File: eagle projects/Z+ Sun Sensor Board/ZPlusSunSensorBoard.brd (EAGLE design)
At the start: 78 x 78 mm, 50 parts, among them U1 TSV991AILT, U2 ADS7841E_2K5, U4 LM20BIM7X_NOPB, U5 TSV991AILT, U8 TSV991AILT

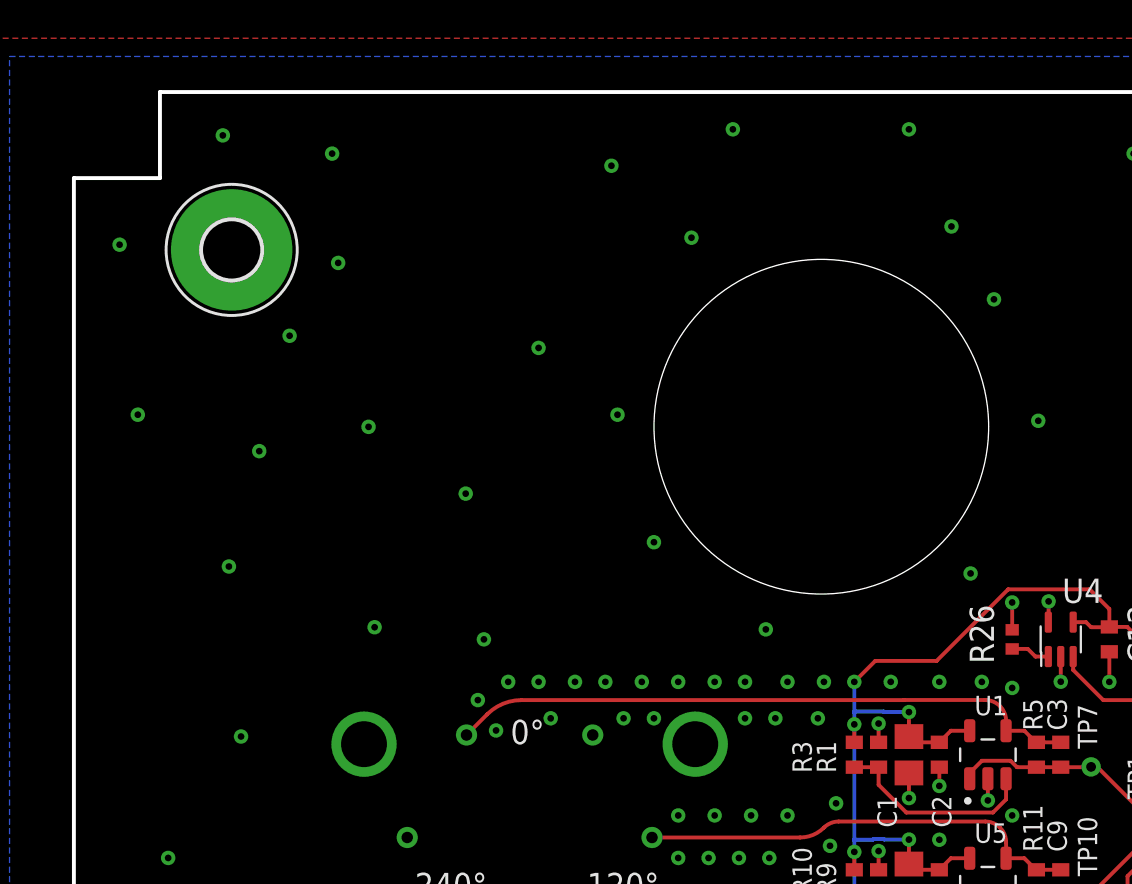
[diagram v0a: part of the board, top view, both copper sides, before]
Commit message: Revert "Added Luc's recommended new power connectors"
This reverts commit dfe48c56fe37fa57a9af7eb032061edffce3900f.
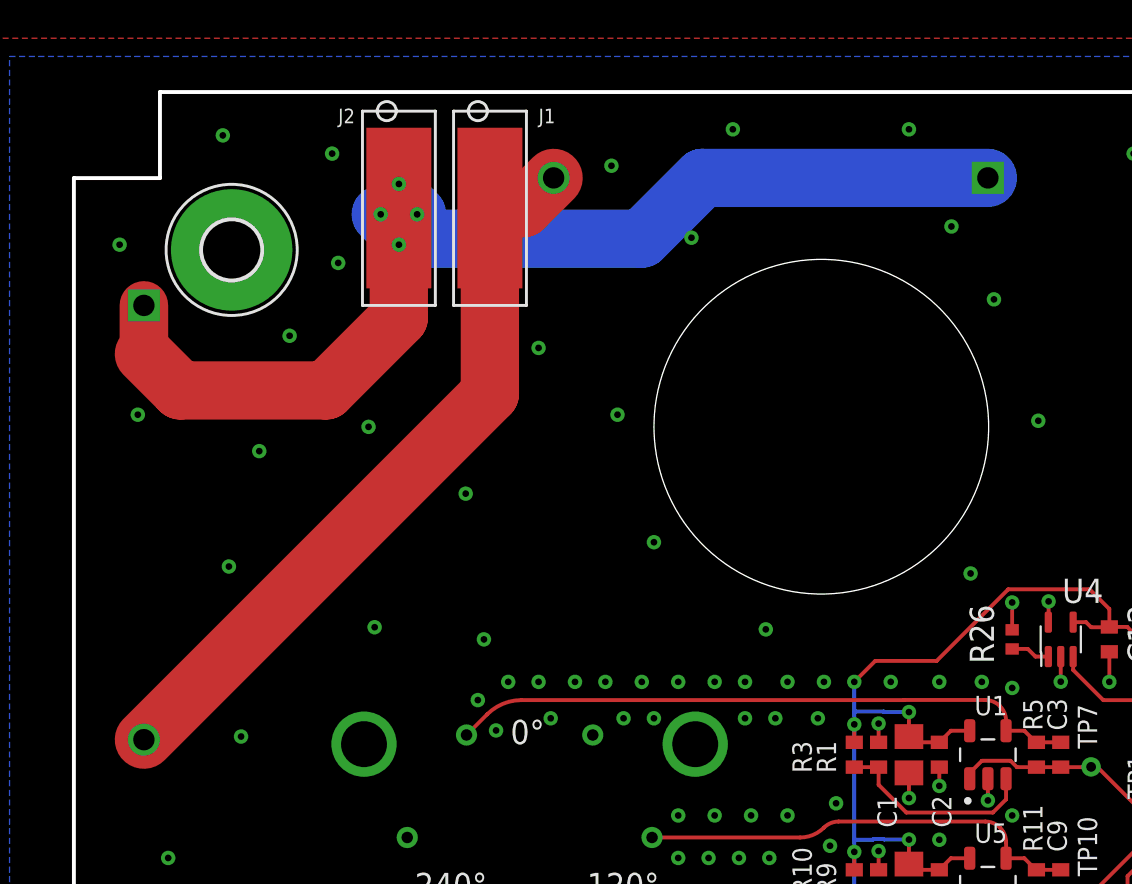
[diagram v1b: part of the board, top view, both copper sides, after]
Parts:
- added J1: Power In, PDUv1:2038638103
- added J2: Power Out, PDUv1:2038638103
- added R6, R7: RS02B2R000FE70, Heating Element:ROX02B_VIS
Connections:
- new net N$5: J1.P$1, R6.2, R7.2
- new net N$6: J2.P$1, R6.1, R7.1
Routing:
- net N$6: track 0.00 -> 61.1 mm, vias 0 -> 4
- net N$5: track 0.00 -> 39.3 mm
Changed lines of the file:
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@@
 <element name="U$3" library="my_library" library_urn="urn:adsk.eagle:library:22876504" package="PHOTODIODE_SILK" package3d_urn="urn:adsk.eagle:package:29580099/1" value="" x="30.48" y="62.865" smashed="yes" rot="MR180"/>
 <element name="U$4" library="my_library" library_urn="urn:adsk.eagle:library:22876504" package="PHOTODIODE_SILK" package3d_urn="urn:adsk.eagle:package:29580099/1" value="" x="45.4025" y="36.5125" smashed="yes" rot="MR300"/>
+<element name="R6" library="Heating Element" library_urn="urn:adsk.eagle:library:29300905" package="ROX02B_VIS" package3d_urn="urn:adsk.eagle:package:29301001/2" value="RS02B2R000FE70" x="54.2925" y="80.01" smashed="yes" rot="MR0">
+<attribute name="BUILT_BY" value="EMA_UL_Team" x="54.2925" y="80.01" size="1.778" layer="28" rot="MR0" display="off"/>
+<attribute name="MANUFACTURER_PART_NUMBER" value="RS02B2R000FE70" x="54.2925" y="80.01" size="1.778" layer="28" rot="MR0" display="off"/>
+<attribute name="NAME" x="48.1203" y="79.375" size="1.27" layer="26" ratio="6" rot="SMR0"/>
+<attribute name="SOURCELIBRARY" value="Vishay_2014-12-31" x="54.2925" y="80.01" size="1.778" layer="28" rot="MR0" display="off"/>
+<attribute name="VENDOR" value="Vishay" x="54.2925" y="80.01" size="1.778" layer="28" rot="MR0" display="off"/>
+</element>
+<element name="R7" library="Heating Element" library_urn="urn:adsk.eagle:library:29300905" package="ROX02B_VIS" package3d_urn="urn:adsk.eagle:package:29301001/2" value="RS02B2R000FE70" x="10.16" y="73.3425" smashed="yes" rot="MR270">
+<attribute name="BUILT_BY" value="EMA_UL_Team" x="10.16" y="73.3425" size="1.778" layer="28" rot="MR270" display="off"/>
+<attribute name="MANUFACTURER_PART_NUMBER" value="RS02B2R000FE70" x="10.16" y="73.3425" size="1.778" layer="28" rot="MR270" display="off"/>
+<attribute name="NAME" x="10.79499375" y="65.2653" size="1.27" layer="26" ratio="6" rot="SMR270"/>
+<attribute name="SOURCELIBRARY" value="Vishay_2014-12-31" x="10.16" y="73.3425" size="1.778" layer="28" rot="MR270" display="off"/>
+<attribute name="VENDOR" value="Vishay" x="10.16" y="73.3425" size="1.778" layer="28" rot="MR270" display="off"/>
+</element>
+<element name="J1" library="PDUv1" library_urn="urn:adsk.eagle:library:29653418" package="2038638103" package3d_urn="urn:adsk.eagle:package:30104253/5" value="Power In" x="26.3525" y="82.2325" smashed="yes" rot="R270">
+<attribute name="NAME" x="30.7975" y="82.8675" size="0.762" layer="25"/>
+<attribute name="VALUE" x="26.67" y="72.39" size="0.762" layer="27"/>
+</element>
+<element name="J2" library="PDUv1" library_urn="urn:adsk.eagle:library:29653418" package="2038638103" package3d_urn="urn:adsk.eagle:package:30104253/5" value="Power Out" x="21.59" y="82.2325" smashed="yes" rot="R270">
+<attribute name="NAME" x="20.32" y="82.8675" size="0.762" layer="25"/>
+<attribute name="VALUE" x="20.6375" y="72.39" size="0.762" layer="27"/>
+</element>
 <element name="JP3" library="830-10-006-20-005000" package="830-10-006-20-005000" value="830-10-006-20-005000" x="75.2475" y="41.5925" smashed="yes" rot="R90">
 <attribute name="AVAILABILITY" value="In Stock" x="75.2475" y="41.5925" size="1.778" layer="27" rot="R90" display="off"/>
@@
 <wire x1="48.5775" y1="35.8625" x2="48.5775" y2="34.94033125" width="0.2032" layer="1"/>
 </signal>
+<signal name="N$5">
+<contactref element="R6" pad="2"/>
+<contactref element="R7" pad="2"/>
+<contactref element="J1" pad="P$1"/>
+<wire x1="31.5849" y1="80.01" x2="30.0074" y2="78.4325" width="3.048" layer="1"/>
+<wire x1="30.0074" y1="78.4325" x2="28.2525" y2="78.4325" width="3.048" layer="1"/>
+<wire x1="28.2525" y1="78.4325" x2="28.2525" y2="68.7274" width="3.048" layer="1"/>
+<wire x1="28.2525" y1="68.7274" x2="10.16" y2="50.6349" width="3.048" layer="1"/>
+</signal>
+<signal name="N$6">
+<contactref element="R6" pad="1"/>
+<contactref element="R7" pad="1"/>
+<via x="23.495" y="79.6925" extent="1-16" drill="0.35"/>
+<via x="24.4475" y="78.105" extent="1-16" drill="0.35"/>
+<via x="23.495" y="76.5175" extent="1-16" drill="0.35"/>
+<via x="22.5425" y="78.105" extent="1-16" drill="0.35"/>
+<wire x1="39.37" y1="80.01" x2="36.195" y2="76.835" width="3.048" layer="16"/>
+<wire x1="36.195" y1="76.835" x2="25.0825" y2="76.835" width="3.048" layer="16"/>
+<wire x1="25.0825" y1="76.835" x2="23.1775" y2="78.74" width="3.048" layer="16"/>
+<wire x1="54.2925" y1="80.01" x2="39.37" y2="80.01" width="3.048" layer="16"/>
+<wire x1="22.5425" y1="78.105" x2="23.495" y2="77.1525" width="3.048" layer="16"/>
+<wire x1="23.495" y1="77.1525" x2="23.495" y2="76.5175" width="3.048" layer="16"/>
+<wire x1="23.495" y1="79.6925" x2="23.495" y2="79.0575" width="3.048" layer="16"/>
+<wire x1="23.495" y1="79.0575" x2="24.4475" y2="78.105" width="3.048" layer="16"/>
+<contactref element="J2" pad="P$1"/>
+<wire x1="23.49" y1="72.7025" x2="19.685" y2="68.8975" width="3.048" layer="1"/>
+<wire x1="23.49" y1="72.7025" x2="23.49" y2="78.4325" width="3.048" layer="1"/>
+<wire x1="12.065" y1="68.8975" x2="10.16" y2="70.8025" width="3.048" layer="1"/>
+<wire x1="19.685" y1="68.8975" x2="12.065" y2="68.8975" width="3.048" layer="1"/>
+<wire x1="10.16" y1="70.8025" x2="10.16" y2="73.3425" width="2.54" layer="1"/>
+<wire x1="23.49" y1="78.4325" x2="23.1775" y2="78.74" width="0" layer="19" extent="1-16"/>
+<wire x1="22.5425" y1="78.105" x2="23.1775" y2="78.74" width="0" layer="19" extent="16-16"/>
+<wire x1="23.495" y1="79.6925" x2="23.1775" y2="78.74" width="0" layer="19" extent="16-16"/>
+</signal>
 <signal name="N$94">
